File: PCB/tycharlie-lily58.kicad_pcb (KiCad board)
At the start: 2 copper layers, 146.4 x 106.9 mm, 78 parts, among them J1 Conn_01x02_Pin, J2 Conn_01x05_Pin, J3 AudioJack4, SW1 SW_Push, SW10 SW_Push, SW11 SW_Push, SW12 SW_Push, SW13 SW_Push, SW14 SW_Push, SW15 SW_Push, SW16 SW_Push, SW17 SW_Push, SW18 SW_Push, SW19 SW_Push, SW2 SW_Push, SW20 SW_Push, SW21 SW_Push, SW22 SW_Push, SW23 SW_Push, SW24 SW_Push, SW25 SW_Push, SW26 SW_Push, SW27 SW_Push, SW28 SW_Push, SW29 SW_Push, SW3 SW_Push, SW30 SW_Push, SW4 SW_Push, SW5 SW_Push, SW6 SW_Push, SW7 SW_Push, SW8 SW_Push, SW9 SW_Push, U1 SuperMini nRF52840

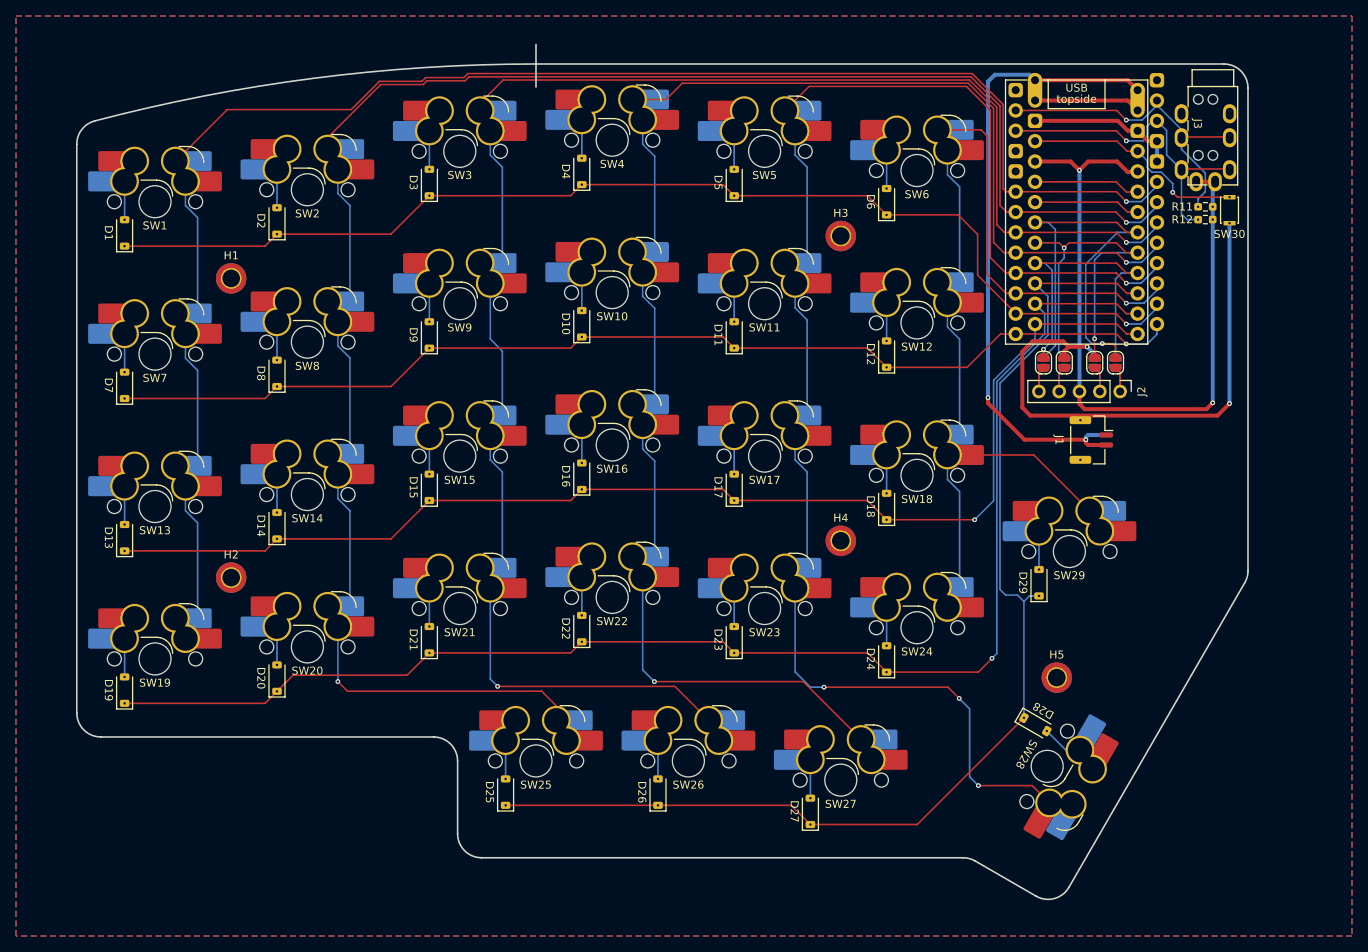
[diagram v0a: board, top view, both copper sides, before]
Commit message: FEAT: add the dxf file for edge cut - use the dxf file to maintain the edge cut - add two different mounting hole - use larger mounting hole for robustness
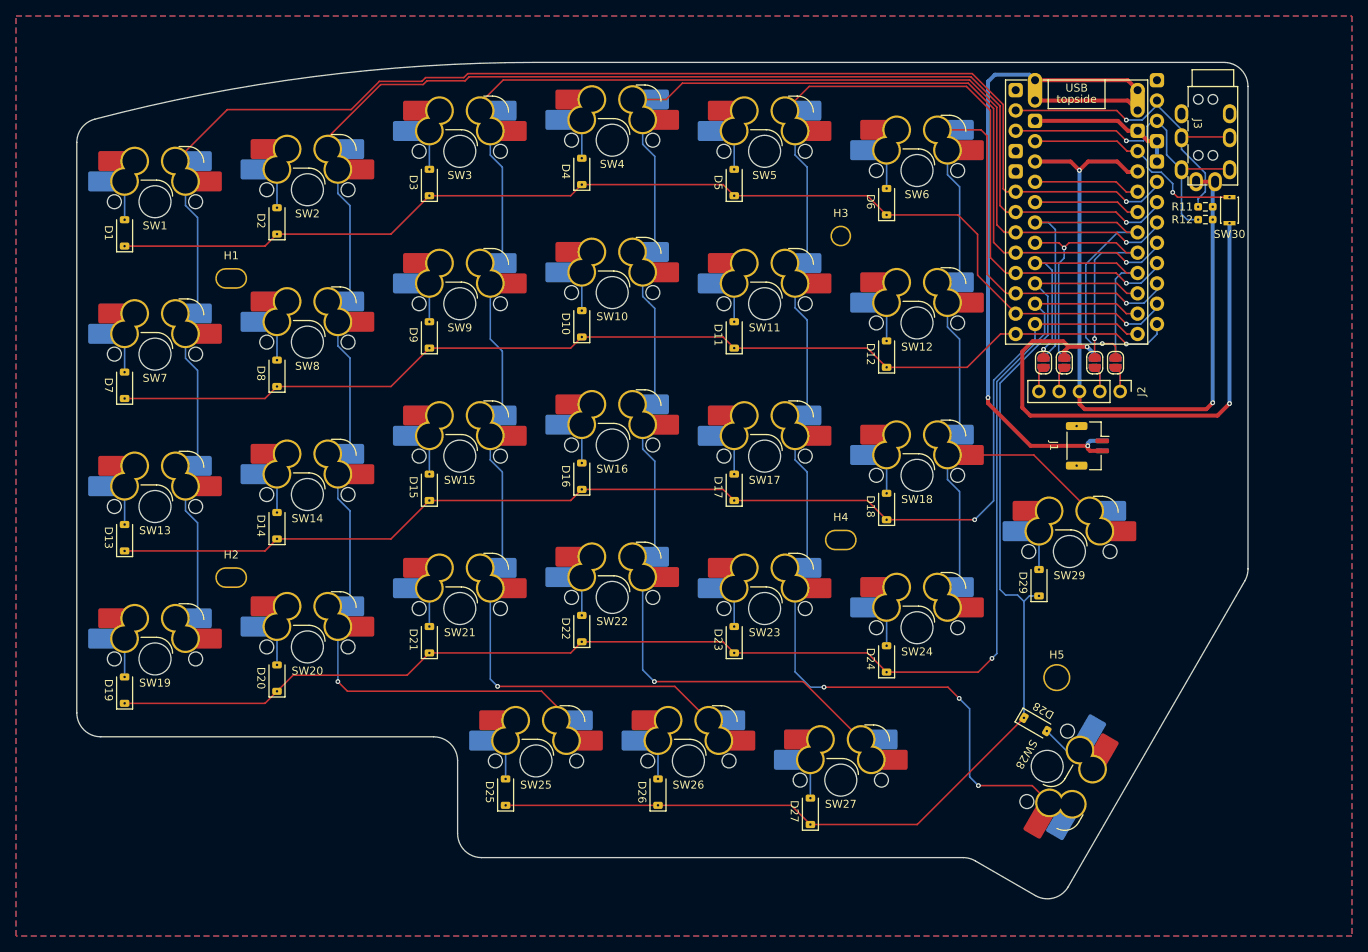
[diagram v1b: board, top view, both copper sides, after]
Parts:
- H1, H2, H4: footprint tycharlie-lily58:MountingHole_2.2mm_M2_ISO14580_Pad_TopBottom -> tycharlie-lily58:MountingHole_3mm_Oval_Hole_ISO14580_Pad_TopBottom
- H5: footprint tycharlie-lily58:MountingHole_2.2mm_M2_ISO14580_Pad_TopBottom -> tycharlie-lily58:MountingHole_3mm_M2_ISO14580_Pad_TopBottom
- moved J1 0.87 mm to (188.0, 76.3)
- moved H4 0.10 mm to (157.2, 88.1)
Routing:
- net +BATT: track 93.5 -> 92.6 mm
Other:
- board size 146.4 x 106.9 mm -> 146.4 x 104.5 mm

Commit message: FIX: fix the group issue the group item in the pcb will not correctly when using the different version, regroup them
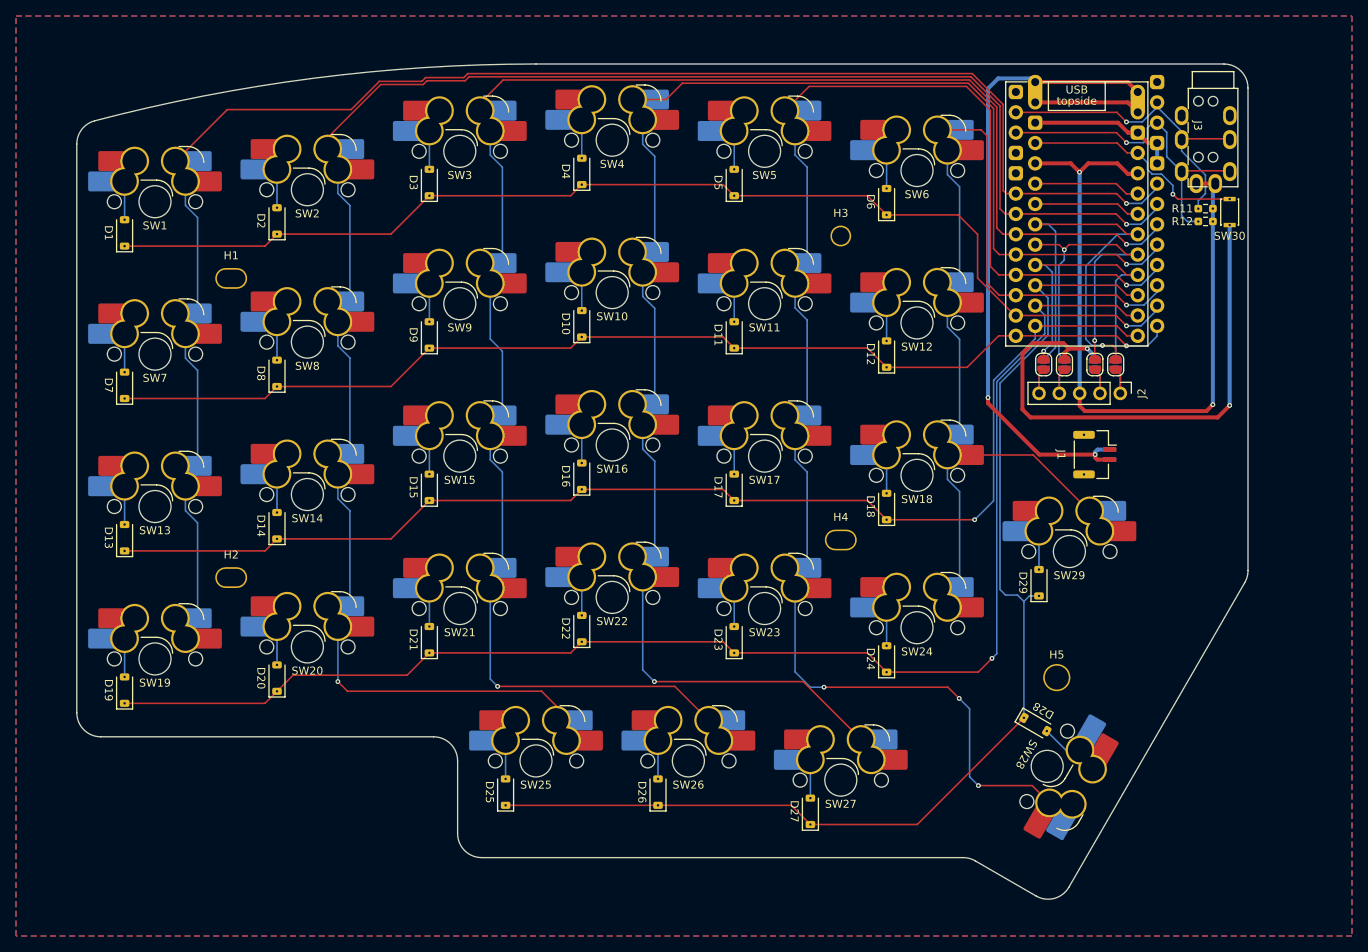
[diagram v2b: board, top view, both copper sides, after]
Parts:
- moved J1 1.43 mm to (188.9, 77.4)
- moved J3 0.23 mm to (202.8, 37.8)
- moved JP1 0.23 mm to (191.5, 66.1)
- moved JP3 0.23 mm to (185.1, 66.1)
- moved JP4 0.23 mm to (182.5, 66.1)
- moved JP5 0.23 mm to (191.5, 66.1)
- moved JP7 0.23 mm to (185.1, 66.1)
- moved JP8 0.23 mm to (182.5, 66.1)
- moved J2 0.23 mm to (192.1, 69.7)
- moved JP2 0.23 mm to (188.9, 66.1)
- moved JP6 0.23 mm to (188.9, 66.1)
- moved R11 0.23 mm to (202.8, 46.7)
- moved R12 0.23 mm to (202.8, 48.3)
- moved U1 0.23 mm to (186.7, 47.4)
- moved SW30 0.23 mm to (205.8, 47.1)
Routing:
- net col_5: track 117.4 -> 118.1 mm
- net col_4: track 175.5 -> 176.3 mm
- net +BATT: track 92.6 -> 93.2 mm
- net col_3: track 180.7 -> 181.3 mm
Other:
- board size 146.4 x 104.5 mm -> 146.4 x 104.4 mm
